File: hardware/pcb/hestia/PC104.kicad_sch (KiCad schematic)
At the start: 2 parts, among them J3 ESQ-126-39-G-D, J4 ESQ-126-39-G-D

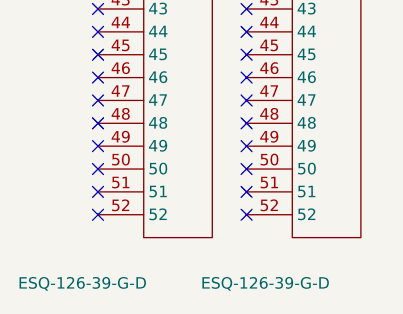
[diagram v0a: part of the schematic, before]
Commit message: edit some component values
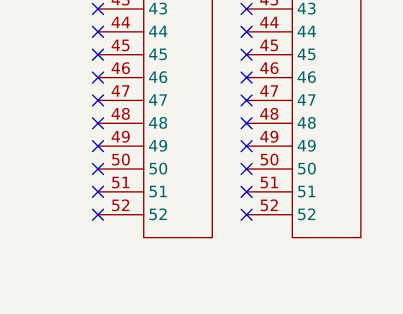
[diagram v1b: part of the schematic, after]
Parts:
- J3, J4: value ESQ-126-39-G-D -> (none); footprint Hestia:ESQ-126-39-G-D -> (none)
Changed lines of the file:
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@@
       (effects (font (size 1.27 1.27)) (justify left))
     )
-    (property "Value" "ESQ-126-39-G-D" (id 1) (at 52.07 162.56 0)
+    (property "Value" "" (id 1) (at 52.07 162.56 0)
       (effects (font (size 1.27 1.27)) (justify left))
     )
-    (property "Footprint" "Hestia:ESQ-126-39-G-D" (id 2) (at 67.31 83.82 0)
+    (property "Footprint" "" (id 2) (at 67.31 83.82 0)
       (effects (font (size 1.27 1.27)) hide)
     )
@@
       (effects (font (size 1.27 1.27)) (justify left))
     )
-    (property "Value" "ESQ-126-39-G-D" (id 1) (at 31.75 162.56 0)
+    (property "Value" "" (id 1) (at 31.75 162.56 0)
       (effects (font (size 1.27 1.27)) (justify left))
     )
-    (property "Footprint" "Hestia:ESQ-126-39-G-D" (id 2) (at 50.8 83.82 0)
+    (property "Footprint" "" (id 2) (at 50.8 83.82 0)
       (effects (font (size 1.27 1.27)) hide)
     )

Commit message: Terminate pin 12 (LDR) on LM2655 to fix ERC warning
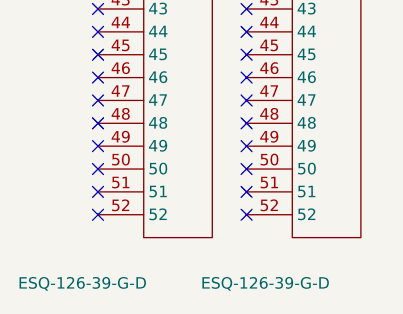
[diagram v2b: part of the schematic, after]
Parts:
- J3, J4: value (none) -> ESQ-126-39-G-D; footprint (none) -> Hestia:ESQ-126-39-G-D
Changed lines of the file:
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@@
       (effects (font (size 1.27 1.27)) (justify left))
     )
-    (property "Value" "" (id 1) (at 52.07 162.56 0)
+    (property "Value" "ESQ-126-39-G-D" (id 1) (at 52.07 162.56 0)
       (effects (font (size 1.27 1.27)) (justify left))
     )
-    (property "Footprint" "" (id 2) (at 67.31 83.82 0)
+    (property "Footprint" "Hestia:ESQ-126-39-G-D" (id 2) (at 67.31 83.82 0)
       (effects (font (size 1.27 1.27)) hide)
     )
@@
       (effects (font (size 1.27 1.27)) (justify left))
     )
-    (property "Value" "" (id 1) (at 31.75 162.56 0)
+    (property "Value" "ESQ-126-39-G-D" (id 1) (at 31.75 162.56 0)
       (effects (font (size 1.27 1.27)) (justify left))
     )
-    (property "Footprint" "" (id 2) (at 50.8 83.82 0)
+    (property "Footprint" "Hestia:ESQ-126-39-G-D" (id 2) (at 50.8 83.82 0)
       (effects (font (size 1.27 1.27)) hide)
     )

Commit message: Bump version to 2.0, add title to all schematic pages
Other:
- company: (none) -> Mawson Rovers
- title: (none) -> Hestia
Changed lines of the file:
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@@
 (kicad_sch (version 20211123) (generator eeschema)
   (paper "A4")
+  (title_block
+    (title "Hestia")
+    (date "2022-07-14")
+    (rev "2.0")
+    (company "Mawson Rovers")
+  )
   (no_connect (at 57.15 53.34))
   (no_connect (at 40.64 114.3))

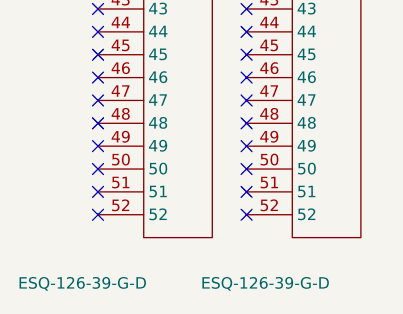
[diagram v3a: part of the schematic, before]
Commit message: added some digikey and mouser part numbers to schematic parts
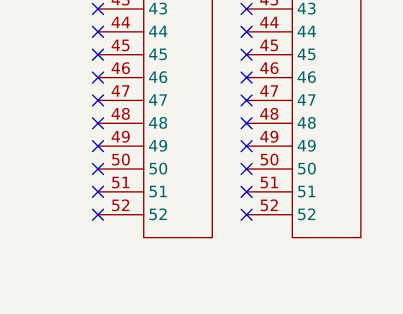
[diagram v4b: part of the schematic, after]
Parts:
- J3, J4: value ESQ-126-39-G-D -> (none); footprint Hestia:ESQ-126-39-G-D -> (none)
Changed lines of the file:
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@@
       (effects (font (size 1.27 1.27)) (justify left))
     )
-    (property "Value" "ESQ-126-39-G-D" (id 1) (at 52.07 162.56 0)
+    (property "Value" "" (id 1) (at 52.07 162.56 0)
       (effects (font (size 1.27 1.27)) (justify left))
     )
-    (property "Footprint" "Hestia:ESQ-126-39-G-D" (id 2) (at 67.31 83.82 0)
+    (property "Footprint" "" (id 2) (at 67.31 83.82 0)
       (effects (font (size 1.27 1.27)) hide)
     )
@@
       (effects (font (size 1.27 1.27)) (justify left))
     )
-    (property "Value" "ESQ-126-39-G-D" (id 1) (at 31.75 162.56 0)
+    (property "Value" "" (id 1) (at 31.75 162.56 0)
       (effects (font (size 1.27 1.27)) (justify left))
     )
-    (property "Footprint" "Hestia:ESQ-126-39-G-D" (id 2) (at 50.8 83.82 0)
+    (property "Footprint" "" (id 2) (at 50.8 83.82 0)
       (effects (font (size 1.27 1.27)) hide)
     )

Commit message: Restore lost footprints in schematics
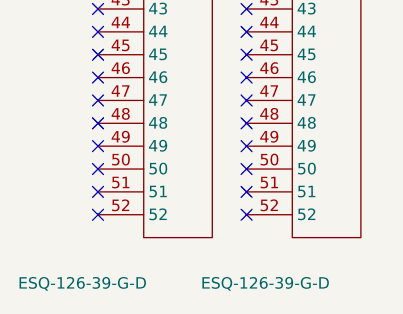
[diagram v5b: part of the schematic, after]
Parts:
- J3, J4: value (none) -> ESQ-126-39-G-D; footprint (none) -> Hestia:ESQ-126-39-G-D
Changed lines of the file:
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@@
       (effects (font (size 1.27 1.27)) (justify left))
     )
-    (property "Value" "" (id 1) (at 52.07 162.56 0)
+    (property "Value" "ESQ-126-39-G-D" (id 1) (at 52.07 162.56 0)
       (effects (font (size 1.27 1.27)) (justify left))
     )
-    (property "Footprint" "" (id 2) (at 67.31 83.82 0)
+    (property "Footprint" "Hestia:ESQ-126-39-G-D" (id 2) (at 67.31 83.82 0)
       (effects (font (size 1.27 1.27)) hide)
     )
@@
       (effects (font (size 1.27 1.27)) (justify left))
     )
-    (property "Value" "" (id 1) (at 31.75 162.56 0)
+    (property "Value" "ESQ-126-39-G-D" (id 1) (at 31.75 162.56 0)
       (effects (font (size 1.27 1.27)) (justify left))
     )
-    (property "Footprint" "" (id 2) (at 50.8 83.82 0)
+    (property "Footprint" "Hestia:ESQ-126-39-G-D" (id 2) (at 50.8 83.82 0)
       (effects (font (size 1.27 1.27)) hide)
     )

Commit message: changed all 10K to 0.5% to be same component. changed led part numbers back to 0805. - my mistake. i had thought the footprints had changed to 0603. filled in other missing digikey part numbers. added manufacturer names and manufacturer part numbers. finished adding SMD/TH entry for component types. Excluded R4/R5 DNP part numbers from BOM
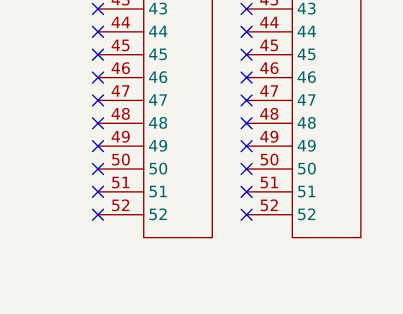
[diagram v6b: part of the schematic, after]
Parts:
- J3, J4: value ESQ-126-39-G-D -> (none); footprint Hestia:ESQ-126-39-G-D -> (none); Type (none) -> TH
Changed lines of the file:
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@@
       (effects (font (size 1.27 1.27)) (justify left))
     )
-    (property "Value" "ESQ-126-39-G-D" (id 1) (at 52.07 162.56 0)
+    (property "Value" "" (id 1) (at 52.07 162.56 0)
       (effects (font (size 1.27 1.27)) (justify left))
     )
-    (property "Footprint" "Hestia:ESQ-126-39-G-D" (id 2) (at 67.31 83.82 0)
+    (property "Footprint" "" (id 2) (at 67.31 83.82 0)
       (effects (font (size 1.27 1.27)) hide)
     )
     (property "Datasheet" "" (id 3) (at 67.31 83.82 0)
+      (effects (font (size 1.27 1.27)) hide)
+    )
+    (property "Type" "TH" (id 4) (at 64.77 88.9 0)
       (effects (font (size 1.27 1.27)) hide)
     )
@@
       (effects (font (size 1.27 1.27)) (justify left))
     )
-    (property "Value" "ESQ-126-39-G-D" (id 1) (at 31.75 162.56 0)
+    (property "Value" "" (id 1) (at 31.75 162.56 0)
       (effects (font (size 1.27 1.27)) (justify left))
     )
-    (property "Footprint" "Hestia:ESQ-126-39-G-D" (id 2) (at 50.8 83.82 0)
+    (property "Footprint" "" (id 2) (at 50.8 83.82 0)
       (effects (font (size 1.27 1.27)) hide)
     )
@@
       (effects (font (size 1.27 1.27)) hide)
     )
+    (property "Type" "TH" (id 4) (at 48.26 88.9 0)
+      (effects (font (size 1.27 1.27)) hide)
+    )

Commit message: c39 digikey and mfr part numbers changed to a 100pf part number. It had previously erroneously been given a 10pf part number
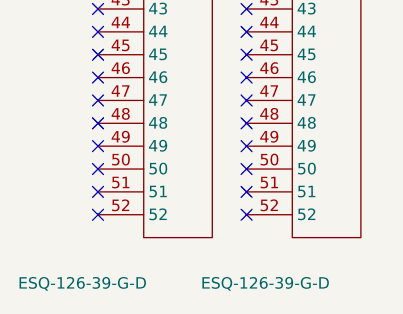
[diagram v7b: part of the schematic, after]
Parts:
- J3, J4: value (none) -> ESQ-126-39-G-D
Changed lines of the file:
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@@
       (effects (font (size 1.27 1.27)) (justify left))
     )
-    (property "Value" "" (id 1) (at 52.07 162.56 0)
+    (property "Value" "ESQ-126-39-G-D" (id 1) (at 52.07 162.56 0)
       (effects (font (size 1.27 1.27)) (justify left))
     )
@@
       (effects (font (size 1.27 1.27)) (justify left))
     )
-    (property "Value" "" (id 1) (at 31.75 162.56 0)
+    (property "Value" "ESQ-126-39-G-D" (id 1) (at 31.75 162.56 0)
       (effects (font (size 1.27 1.27)) (justify left))
     )

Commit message: change d6? to SK34A-LTP with a DO-214AC (SMA) footprint. This diode is a higher profile and may violate height restrictions for some close stacked payload configurations.
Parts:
- J3, J4: footprint (none) -> Hestia:ESQ-126-39-G-D
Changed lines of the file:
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@@
       (effects (font (size 1.27 1.27)) (justify left))
     )
-    (property "Footprint" "" (id 2) (at 67.31 83.82 0)
+    (property "Footprint" "Hestia:ESQ-126-39-G-D" (id 2) (at 67.31 83.82 0)
       (effects (font (size 1.27 1.27)) hide)
     )
@@
       (effects (font (size 1.27 1.27)) (justify left))
     )
-    (property "Footprint" "" (id 2) (at 50.8 83.82 0)
+    (property "Footprint" "Hestia:ESQ-126-39-G-D" (id 2) (at 50.8 83.82 0)
       (effects (font (size 1.27 1.27)) hide)
     )
